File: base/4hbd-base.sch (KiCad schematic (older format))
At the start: 33 parts

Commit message: annotate sch
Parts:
- gave numbers to parts that had none: 33

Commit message: added footprints, created netlist
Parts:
- J8: footprint (none) -> TerminalBlock:SpringTerminalBlock_KF141R_4_P2.54mm
- TP1, TP10, TP11, TP12, TP13, TP14, TP15, TP16, TP17, TP18, TP19, TP2, TP20, TP3, TP4, TP5, TP6, TP7, TP8, TP9: footprint (none) -> TestPoint:TestPoint_Pad_D1.5mm

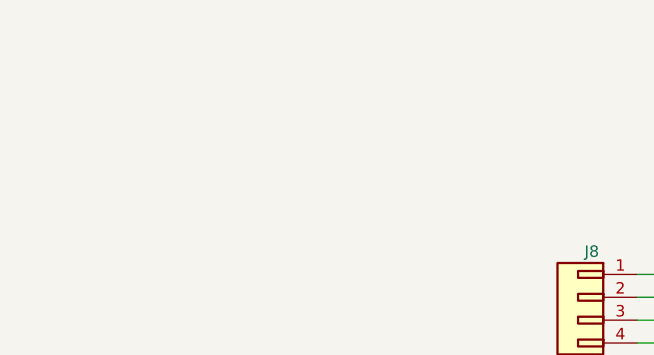
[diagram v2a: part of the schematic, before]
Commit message: mount hole was added
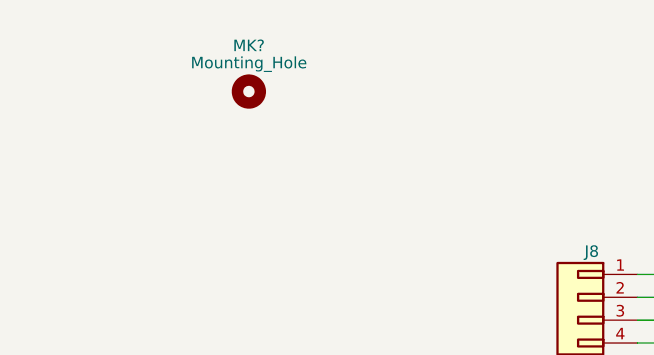
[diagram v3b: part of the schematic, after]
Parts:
- added MK?: Mounting_Hole, symbol Mounting_Hole
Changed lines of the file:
@@
 LIBS:opto
 LIBS:maxim
+LIBS:Mechanical
 LIBS:4hbd-base-cache
 EELAYER 25 0
@@
 	1    0    0    -1
 $EndComp
+$Comp
+L Mounting_Hole MK?
+U 1 1 5A4C234B
+P 900 900
+F 0 "MK?" H 900 1100 50  0000 C CNN
+F 1 "Mounting_Hole" H 900 1025 50  0000 C CNN
+F 2 "" H 900 900 50  0001 C CNN
+F 3 "" H 900 900 50  0001 C CNN
+	1    900  900
+	1    0    0    -1
+$EndComp

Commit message: mount hole
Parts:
- removed J8: Spring_Terminal_Connector_01x04, TerminalBlock:SpringTerminalBlock_KF141R_4_P2.54mm, symbol Spring_Terminal_Connector_01x04
- added J8: Screw_Terminal_01x04, TerminalBlock:TerminalBlock_Altech_AK300-4_P5.00mm, symbol Screw_Terminal_01x04
- added MK2, MK3, MK4: Mounting_Hole, MountingHole:MountingHole_3.5mm_Pad, symbol Mounting_Hole
- MK1: renamed from MK?; footprint (none) -> MountingHole:MountingHole_3.5mm_Pad
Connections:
- net MOSFETs/CurSense/Isolation/HB0s: now also J8.1 (Pin_1)
- net MOSFETs/CurSense/Isolation/HB1: now also J8.2 (Pin_2)
- net MOSFETs/CurSense/Isolation/HB2s: now also J8.3 (Pin_3)
- net MOSFETs/CurSense/Isolation/HB3: now also J8.4 (Pin_4)
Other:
- moved on the sheet: MK1
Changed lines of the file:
@@
 $EndSheet
 $Comp
-L GNDD #PWR01
+L GNDD #PWR12
 U 1 1 5A1C4DF7
 P 8900 6000
-F 0 "#PWR01" H 8900 5750 50  0001 C CNN
+F 0 "#PWR12" H 8900 5750 50  0001 C CNN
 F 1 "GNDD" H 8900 5875 50  0000 C CNN
 F 2 "" H 8900 6000 50  0001 C CNN
@@
 $EndComp
 $Comp
-L GNDD #PWR02
+L GNDD #PWR11
 U 1 1 5A1C5052
 P 8900 3500
-F 0 "#PWR02" H 8900 3250 50  0001 C CNN
+F 0 "#PWR11" H 8900 3250 50  0001 C CNN
 F 1 "GNDD" H 8900 3375 50  0000 C CNN
 F 2 "" H 8900 3500 50  0001 C CNN
@@
 $EndComp
 $Comp
-L GNDD #PWR03
+L GNDD #PWR7
 U 1 1 5A1C5445
 P 4800 5600
-F 0 "#PWR03" H 4800 5350 50  0001 C CNN
+F 0 "#PWR7" H 4800 5350 50  0001 C CNN
 F 1 "GNDD" H 4800 5475 50  0000 C CNN
 F 2 "" H 4800 5600 50  0001 C CNN
@@
 $EndComp
 $Comp
-L GNDD #PWR04
+L GNDD #PWR6
 U 1 1 5A1C7749
 P 4800 3800
-F 0 "#PWR04" H 4800 3550 50  0001 C CNN
+F 0 "#PWR6" H 4800 3550 50  0001 C CNN
 F 1 "GNDD" H 4800 3675 50  0000 C CNN
 F 2 "" H 4800 3800 50  0001 C CNN
@@
 $EndComp
 $Comp
-L GNDD #PWR05
+L GNDD #PWR10
 U 1 1 5A1D2700
 P 8400 4800
-F 0 "#PWR05" H 8400 4550 50  0001 C CNN
+F 0 "#PWR10" H 8400 4550 50  0001 C CNN
 F 1 "GNDD" H 8400 4675 50  0000 C CNN
 F 2 "" H 8400 4800 50  0001 C CNN
@@
 $EndComp
 $Comp
-L GNDD #PWR06
+L GNDD #PWR15
 U 1 1 5A1D7E7F
 P 10650 5500
-F 0 "#PWR06" H 10650 5250 50  0001 C CNN
+F 0 "#PWR15" H 10650 5250 50  0001 C CNN
 F 1 "GNDD" H 10650 5375 50  0000 C CNN
 F 2 "" H 10650 5500 50  0001 C CNN
@@
 $EndSheet
 $Comp
-L GNDD #PWR07
+L GNDD #PWR14
 U 1 1 5A1E3D1F
 P 10600 2500
-F 0 "#PWR07" H 10600 2250 50  0001 C CNN
+F 0 "#PWR14" H 10600 2250 50  0001 C CNN
 F 1 "GNDD" H 10600 2375 50  0000 C CNN
 F 2 "" H 10600 2500 50  0001 C CNN
@@
 $EndComp
 $Comp
-L GNDD #PWR08
+L GNDD #PWR13
 U 1 1 5A1E950D
 P 10200 1750
-F 0 "#PWR08" H 10200 1500 50  0001 C CNN
+F 0 "#PWR13" H 10200 1500 50  0001 C CNN
 F 1 "GNDD" H 10200 1625 50  0000 C CNN
 F 2 "" H 10200 1750 50  0001 C CNN
@@
 $EndComp
 $Comp
-L GNDPWR #PWR09
+L GNDPWR #PWR3
 U 1 1 5A1F43A1
 P 2800 5600
-F 0 "#PWR09" H 2800 5400 50  0001 C CNN
+F 0 "#PWR3" H 2800 5400 50  0001 C CNN
 F 1 "GNDPWR" H 2800 5470 50  0000 C CNN
 F 2 "" H 2800 5550 50  0001 C CNN
@@
 $EndComp
 $Comp
-L GNDPWR #PWR010
+L GNDPWR #PWR1
 U 1 1 5A1F4674
 P 1200 7100
-F 0 "#PWR010" H 1200 6900 50  0001 C CNN
+F 0 "#PWR1" H 1200 6900 50  0001 C CNN
 F 1 "GNDPWR" H 1200 6970 50  0000 C CNN
 F 2 "" H 1200 7050 50  0001 C CNN
@@
 $EndComp
 $Comp
-L GNDPWR #PWR011
+L GNDPWR #PWR2
 U 1 1 5A1F4ECF
 P 2800 3600
-F 0 "#PWR011" H 2800 3400 50  0001 C CNN
+F 0 "#PWR2" H 2800 3400 50  0001 C CNN
 F 1 "GNDPWR" H 2800 3470 50  0000 C CNN
 F 2 "" H 2800 3550 50  0001 C CNN
@@
 $EndSheet
 $Comp
-L GNDD #PWR012
+L GNDD #PWR8
 U 1 1 5A3B40B0
 P 6200 7400
-F 0 "#PWR012" H 6200 7150 50  0001 C CNN
+F 0 "#PWR8" H 6200 7150 50  0001 C CNN
 F 1 "GNDD" H 6200 7275 50  0000 C CNN
 F 2 "" H 6200 7400 50  0001 C CNN
@@
 $EndComp
 $Comp
-L GNDD #PWR013
+L GNDD #PWR5
 U 1 1 5A3B43A6
 P 4600 7000
-F 0 "#PWR013" H 4600 6750 50  0001 C CNN
+F 0 "#PWR5" H 4600 6750 50  0001 C CNN
 F 1 "GNDD" H 4600 6875 50  0000 C CNN
 F 2 "" H 4600 7000 50  0001 C CNN
@@
 Connection ~ 5100 1400
 $Comp
-L GNDD #PWR014
+L GNDD #PWR9
 U 1 1 5A497DD0
 P 7950 6350
-F 0 "#PWR014" H 7950 6100 50  0001 C CNN
+F 0 "#PWR9" H 7950 6100 50  0001 C CNN
 F 1 "GNDD" H 7950 6225 50  0000 C CNN
 F 2 "" H 7950 6350 50  0001 C CNN
@@
 Connection ~ 2850 7400
 $Comp
-L GNDPWR #PWR015
+L GNDPWR #PWR4
 U 1 1 5A49D4A5
 P 3100 7500
-F 0 "#PWR015" H 3100 7300 50  0001 C CNN
+F 0 "#PWR4" H 3100 7300 50  0001 C CNN
 F 1 "GNDPWR" H 3100 7370 50  0000 C CNN
 F 2 "" H 3100 7450 50  0001 C CNN
@@
 $EndComp
 $Comp
-L Spring_Terminal_Connector_01x04 J8
-U 1 1 5A4C5A2B
-P 2400 1800
-F 0 "J8" H 2400 2000 50  0000 C CNN
-F 1 "Spring_Terminal_Connector_01x04" H 2450 1500 50  0000 C CNN
-F 2 "TerminalBlock:SpringTerminalBlock_KF141R_4_P2.54mm" H 2400 1800 50  0001 C CNN
-F 3 "" H 2400 1800 50  0001 C CNN
-	1    2400 1800
-	-1   0    0    -1
-$EndComp
-$Comp
 L Spring_Terminal_Connector_01x08 J12
 U 1 1 5A4CBF24
@@
 $EndComp
 $Comp
-L Mounting_Hole MK?
+L Mounting_Hole MK1
 U 1 1 5A4C234B
-P 900 900
-F 0 "MK?" H 900 1100 50  0000 C CNN
-F 1 "Mounting_Hole" H 900 1025 50  0000 C CNN
-F 2 "" H 900 900 50  0001 C CNN
-F 3 "" H 900 900 50  0001 C CNN
-	1    900  900
-	1    0    0    -1
-$EndComp
+P 850 950
+F 0 "MK1" H 850 1150 50  0000 C CNN
+F 1 "Mounting_Hole" H 850 1075 50  0000 C CNN
+F 2 "MountingHole:MountingHole_3.5mm_Pad" H 850 950 50  0001 C CNN
+F 3 "" H 850 950 50  0001 C CNN
+	1    850  950
+	1    0    0    -1
+$EndComp
+$Comp
+L Screw_Terminal_01x04 J8
+U 1 1 5A4F1133
+P 2400 1800
+F 0 "J8" H 2400 2000 50  0000 C CNN
+F 1 "Screw_Terminal_01x04" H 2400 1500 50  0000 C CNN
+F 2 "TerminalBlock:TerminalBlock_Altech_AK300-4_P5.00mm" H 2400 1800 50  0001 C CNN
+F 3 "" H 2400 1800 50  0001 C CNN
+	1    2400 1800
+	-1   0    0    -1
+$EndComp
+$Comp
+L Mounting_Hole MK2
+U 1 1 5A4F295C
+P 850 1350
+F 0 "MK2" H 850 1550 50  0000 C CNN
+F 1 "Mounting_Hole" H 850 1475 50  0000 C CNN
+F 2 "MountingHole:MountingHole_3.5mm_Pad" H 850 1350 50  0001 C CNN
+F 3 "" H 850 1350 50  0001 C CNN
+	1    850  1350
+	1    0    0    -1
+$EndComp
+$Comp
+L Mounting_Hole MK3
+U 1 1 5A4F2CD9
+P 850 1750
+F 0 "MK3" H 850 1950 50  0000 C CNN
+F 1 "Mounting_Hole" H 850 1875 50  0000 C CNN
+F 2 "MountingHole:MountingHole_3.5mm_Pad" H 850 1750 50  0001 C CNN
+F 3 "" H 850 1750 50  0001 C CNN
+	1    850  1750
+	1    0    0    -1
+$EndComp
+$Comp
+L Mounting_Hole MK4
+U 1 1 5A4F3055
+P 850 2150
+F 0 "MK4" H 850 2350 50  0000 C CNN
+F 1 "Mounting_Hole" H 850 2275 50  0000 C CNN
+F 2 "MountingHole:MountingHole_3.5mm_Pad" H 850 2150 50  0001 C CNN
+F 3 "" H 850 2150 50  0001 C CNN
+	1    850  2150
+	1    0    0    -1
+$EndComp

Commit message: update pcb for TerminalBlock_KaiFeng footprint lib
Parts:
- J1, J10, J11, J2, J3, J4, J9: footprint TerminalBlock:SpringTerminalBlock_KF141R_3_P2.54mm -> TerminalBlock_KaiFeng:TerminalBlock_KaiFeng_KF141R-3_1x03_P2.54mm
- J12: footprint TerminalBlock:SpringTerminalBlock_KF141R_8_P2.54mm -> TerminalBlock_KaiFeng:TerminalBlock_KaiFeng_KF141R-8_1x08_P2.54mm
- J5, J6: footprint TerminalBlock:SpringTerminalBlock_KF141R_2_P2.54mm -> TerminalBlock_KaiFeng:TerminalBlock_KaiFeng_KF141R-2_1x02_P2.54mm
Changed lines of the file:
@@
 F 0 "J1" H 700 3600 50  0000 C CNN
 F 1 "Spring_Terminal_Connector_01x03" H 700 3200 50  0000 C CNN
-F 2 "TerminalBlock:SpringTerminalBlock_KF141R_3_P2.54mm" H 700 3400 50  0001 C CNN
+F 2 "TerminalBlock_KaiFeng:TerminalBlock_KaiFeng_KF141R-3_1x03_P2.54mm" H 700 3400 50  0001 C CNN
 F 3 "" H 700 3400 50  0001 C CNN
 	1    700  3400
@@
 F 0 "J2" H 700 4000 50  0000 C CNN
 F 1 "Spring_Terminal_Connector_01x03" H 700 3600 50  0000 C CNN
-F 2 "TerminalBlock:SpringTerminalBlock_KF141R_3_P2.54mm" H 700 3800 50  0001 C CNN
+F 2 "TerminalBlock_KaiFeng:TerminalBlock_KaiFeng_KF141R-3_1x03_P2.54mm" H 700 3800 50  0001 C CNN
 F 3 "" H 700 3800 50  0001 C CNN
 	1    700  3800
@@
 F 0 "J3" H 700 4400 50  0000 C CNN
 F 1 "Spring_Terminal_Connector_01x03" H 700 4000 50  0000 C CNN
-F 2 "TerminalBlock:SpringTerminalBlock_KF141R_3_P2.54mm" H 700 4200 50  0001 C CNN
+F 2 "TerminalBlock_KaiFeng:TerminalBlock_KaiFeng_KF141R-3_1x03_P2.54mm" H 700 4200 50  0001 C CNN
 F 3 "" H 700 4200 50  0001 C CNN
 	1    700  4200
@@
 F 0 "J4" H 700 4800 50  0000 C CNN
 F 1 "Spring_Terminal_Connector_01x03" H 700 4400 50  0000 C CNN
-F 2 "TerminalBlock:SpringTerminalBlock_KF141R_3_P2.54mm" H 700 4600 50  0001 C CNN
+F 2 "TerminalBlock_KaiFeng:TerminalBlock_KaiFeng_KF141R-3_1x03_P2.54mm" H 700 4600 50  0001 C CNN
 F 3 "" H 700 4600 50  0001 C CNN
 	1    700  4600
@@
 F 0 "J9" H 4300 6500 50  0000 C CNN
 F 1 "Spring_Terminal_Connector_01x03" H 4300 6100 50  0000 C CNN
-F 2 "TerminalBlock:SpringTerminalBlock_KF141R_3_P2.54mm" H 4300 6300 50  0001 C CNN
+F 2 "TerminalBlock_KaiFeng:TerminalBlock_KaiFeng_KF141R-3_1x03_P2.54mm" H 4300 6300 50  0001 C CNN
 F 3 "" H 4300 6300 50  0001 C CNN
 	1    4300 6300
@@
 F 0 "J10" H 4300 6900 50  0000 C CNN
 F 1 "Spring_Terminal_Connector_01x03" H 4300 6500 50  0000 C CNN
-F 2 "TerminalBlock:SpringTerminalBlock_KF141R_3_P2.54mm" H 4300 6700 50  0001 C CNN
+F 2 "TerminalBlock_KaiFeng:TerminalBlock_KaiFeng_KF141R-3_1x03_P2.54mm" H 4300 6700 50  0001 C CNN
 F 3 "" H 4300 6700 50  0001 C CNN
 	1    4300 6700
@@
 F 0 "J11" H 10900 1400 50  0000 C CNN
 F 1 "Spring_Terminal_Connector_01x03" H 10900 1000 50  0000 C CNN
-F 2 "TerminalBlock:SpringTerminalBlock_KF141R_3_P2.54mm" H 10900 1200 50  0001 C CNN
+F 2 "TerminalBlock_KaiFeng:TerminalBlock_KaiFeng_KF141R-3_1x03_P2.54mm" H 10900 1200 50  0001 C CNN
 F 3 "" H 10900 1200 50  0001 C CNN
 	1    10900 1200
@@
 F 0 "J12" H 10900 2700 50  0000 C CNN
 F 1 "Spring_Terminal_Connector_01x08" H 10950 1750 50  0000 C CNN
-F 2 "TerminalBlock:SpringTerminalBlock_KF141R_8_P2.54mm" H 10900 2500 50  0001 C CNN
+F 2 "TerminalBlock_KaiFeng:TerminalBlock_KaiFeng_KF141R-8_1x08_P2.54mm" H 10900 2500 50  0001 C CNN
 F 3 "" H 10900 2500 50  0001 C CNN
 	1    10900 2500
@@
 F 0 "J5" H 700 5200 50  0000 C CNN
 F 1 "Spring_Terminal_Connector_01x02" H 750 4900 50  0000 C CNN
-F 2 "TerminalBlock:SpringTerminalBlock_KF141R_2_P2.54mm" H 700 5000 50  0001 C CNN
+F 2 "TerminalBlock_KaiFeng:TerminalBlock_KaiFeng_KF141R-2_1x02_P2.54mm" H 700 5000 50  0001 C CNN
 F 3 "" H 700 5000 50  0001 C CNN
 	1    700  5000
@@
 F 0 "J6" H 700 5500 50  0000 C CNN
 F 1 "Spring_Terminal_Connector_01x02" H 750 5200 50  0000 C CNN
-F 2 "TerminalBlock:SpringTerminalBlock_KF141R_2_P2.54mm" H 700 5300 50  0001 C CNN
+F 2 "TerminalBlock_KaiFeng:TerminalBlock_KaiFeng_KF141R-2_1x02_P2.54mm" H 700 5300 50  0001 C CNN
 F 3 "" H 700 5300 50  0001 C CNN
 	1    700  5300

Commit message: pcb was edited
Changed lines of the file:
@@
 P 700 3400
 F 0 "J1" H 700 3600 50  0000 C CNN
-F 1 "Spring_Terminal_Connector_01x03" H 700 3200 50  0000 C CNN
+F 1 "Spring_Terminal_Connector_01x03" H 1500 3200 50  0000 C CNN
 F 2 "TerminalBlock_KaiFeng:TerminalBlock_KaiFeng_KF141R-3_1x03_P2.54mm" H 700 3400 50  0001 C CNN
 F 3 "" H 700 3400 50  0001 C CNN
@@
 P 700 3800
 F 0 "J2" H 700 4000 50  0000 C CNN
-F 1 "Spring_Terminal_Connector_01x03" H 700 3600 50  0000 C CNN
+F 1 "Spring_Terminal_Connector_01x03" H 1500 3600 50  0000 C CNN
 F 2 "TerminalBlock_KaiFeng:TerminalBlock_KaiFeng_KF141R-3_1x03_P2.54mm" H 700 3800 50  0001 C CNN
 F 3 "" H 700 3800 50  0001 C CNN
@@
 P 700 4200
 F 0 "J3" H 700 4400 50  0000 C CNN
-F 1 "Spring_Terminal_Connector_01x03" H 700 4000 50  0000 C CNN
+F 1 "Spring_Terminal_Connector_01x03" H 1500 4000 50  0000 C CNN
 F 2 "TerminalBlock_KaiFeng:TerminalBlock_KaiFeng_KF141R-3_1x03_P2.54mm" H 700 4200 50  0001 C CNN
 F 3 "" H 700 4200 50  0001 C CNN
@@
 P 700 4600
 F 0 "J4" H 700 4800 50  0000 C CNN
-F 1 "Spring_Terminal_Connector_01x03" H 700 4400 50  0000 C CNN
+F 1 "Spring_Terminal_Connector_01x03" H 1500 4400 50  0000 C CNN
 F 2 "TerminalBlock_KaiFeng:TerminalBlock_KaiFeng_KF141R-3_1x03_P2.54mm" H 700 4600 50  0001 C CNN
 F 3 "" H 700 4600 50  0001 C CNN
@@
 P 4300 6300
 F 0 "J9" H 4300 6500 50  0000 C CNN
-F 1 "Spring_Terminal_Connector_01x03" H 4300 6100 50  0000 C CNN
+F 1 "Spring_Terminal_Connector_01x03" H 5050 6100 50  0000 C CNN
 F 2 "TerminalBlock_KaiFeng:TerminalBlock_KaiFeng_KF141R-3_1x03_P2.54mm" H 4300 6300 50  0001 C CNN
 F 3 "" H 4300 6300 50  0001 C CNN
@@
 P 4300 6700
 F 0 "J10" H 4300 6900 50  0000 C CNN
-F 1 "Spring_Terminal_Connector_01x03" H 4300 6500 50  0000 C CNN
+F 1 "Spring_Terminal_Connector_01x03" H 4750 6500 50  0000 C CNN
 F 2 "TerminalBlock_KaiFeng:TerminalBlock_KaiFeng_KF141R-3_1x03_P2.54mm" H 4300 6700 50  0001 C CNN
 F 3 "" H 4300 6700 50  0001 C CNN
@@
 P 700 5000
 F 0 "J5" H 700 5200 50  0000 C CNN
-F 1 "Spring_Terminal_Connector_01x02" H 750 4900 50  0000 C CNN
+F 1 "Spring_Terminal_Connector_01x02" H 1500 4900 50  0000 C CNN
 F 2 "TerminalBlock_KaiFeng:TerminalBlock_KaiFeng_KF141R-2_1x02_P2.54mm" H 700 5000 50  0001 C CNN
 F 3 "" H 700 5000 50  0001 C CNN
@@
 P 700 5300
 F 0 "J6" H 700 5500 50  0000 C CNN
-F 1 "Spring_Terminal_Connector_01x02" H 750 5200 50  0000 C CNN
+F 1 "Spring_Terminal_Connector_01x02" H 1500 5200 50  0000 C CNN
 F 2 "TerminalBlock_KaiFeng:TerminalBlock_KaiFeng_KF141R-2_1x02_P2.54mm" H 700 5300 50  0001 C CNN
 F 3 "" H 700 5300 50  0001 C CNN

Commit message: current pcb
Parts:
- MK1, MK2, MK3, MK4: footprint MountingHole:MountingHole_3.5mm_Pad -> MountingHole:MountingHole_3.5mm
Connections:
- net Digital DC/DC/+24VD: now also J13.2 (Pin_2); no longer J13.1 (Pin_1)
- net GNDD: now also J13.1 (Pin_1); no longer J13.2 (Pin_2)
- net GNDPWR: now also J7.1 (Pin_1); no longer J7.3 (Pin_3)
- net MOSFETs/CurSense/Isolation/Vpwr: now also J7.2 (Pin_2); no longer J7.1 (Pin_1)
- net Power DC/DC/+24VP: now also J7.3 (Pin_3); no longer J7.2 (Pin_2)
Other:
- moved on the sheet: J13
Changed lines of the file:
@@
 L GNDD #PWR06
 U 1 1 5A1D7E7F
-P 10650 5500
-F 0 "#PWR06" H 10650 5250 50  0001 C CNN
-F 1 "GNDD" H 10650 5375 50  0000 C CNN
-F 2 "" H 10650 5500 50  0001 C CNN
-F 3 "" H 10650 5500 50  0001 C CNN
-	1    10650 5500
+P 10700 5150
+F 0 "#PWR06" H 10700 4900 50  0001 C CNN
+F 1 "GNDD" H 10700 5025 50  0000 C CNN
+F 2 "" H 10700 5150 50  0001 C CNN
+F 3 "" H 10700 5150 50  0001 C CNN
+	1    10700 5150
 	0    1    1    0
 $EndComp
@@
 	9100 2900 8200 2900
 Wire Wire Line
-	10300 5400 10750 5400
-Wire Wire Line
-	10750 5500 10650 5500
-Wire Wire Line
 	4600 3300 6900 3300
 Wire Wire Line
@@
 	2800 5500 2800 5600
 Wire Wire Line
-	1200 7000 1400 7000
+	950  7000 1400 7000
 Wire Wire Line
 	2600 6800 2300 6800
@@
 	2500 3300 3000 3300
 Wire Wire Line
-	1300 6800 900  6800
-Wire Wire Line
-	900  6700 1400 6700
-Wire Wire Line
-	900  6600 1100 6600
-Wire Wire Line
-	1100 6600 1100 3200
+	1100 3200 1100 6500
 Wire Wire Line
 	1100 3200 3000 3200
@@
 	2600 2000 3000 2000
 Wire Wire Line
-	1200 7000 1200 7100
-Wire Wire Line
-	1300 3500 1300 7000
+	1300 3500 1300 7100
 Connection ~ 1300 7000
-Connection ~ 1300 6800
 Wire Wire Line
 	1200 3300 1200 6700
@@
 L Screw_Terminal_01x02 J13
 U 1 1 5A4C5EB8
-P 10950 5400
-F 0 "J13" H 10950 5500 50  0000 C CNN
-F 1 "Screw_Terminal_01x02" H 10950 5200 50  0000 C CNN
-F 2 "TerminalBlock:TerminalBlock_Altech_AK300-2_P5.00mm" H 10950 5400 50  0001 C CNN
-F 3 "" H 10950 5400 50  0001 C CNN
-	1    10950 5400
+P 10950 5300
+F 0 "J13" H 10950 5400 50  0000 C CNN
+F 1 "Screw_Terminal_01x02" H 10950 5100 50  0000 C CNN
+F 2 "TerminalBlock:TerminalBlock_Altech_AK300-2_P5.00mm" H 10950 5300 50  0001 C CNN
+F 3 "" H 10950 5300 50  0001 C CNN
+	1    10950 5300
 	1    0    0    -1
 $EndComp
@@
 F 0 "MK1" H 850 1150 50  0000 C CNN
 F 1 "Mounting_Hole" H 850 1075 50  0000 C CNN
-F 2 "MountingHole:MountingHole_3.5mm_Pad" H 850 950 50  0001 C CNN
+F 2 "MountingHole:MountingHole_3.5mm" H 850 950 50  0001 C CNN
 F 3 "" H 850 950 50  0001 C CNN
 	1    850  950
@@
 F 0 "MK2" H 850 1550 50  0000 C CNN
 F 1 "Mounting_Hole" H 850 1475 50  0000 C CNN
-F 2 "MountingHole:MountingHole_3.5mm_Pad" H 850 1350 50  0001 C CNN
+F 2 "MountingHole:MountingHole_3.5mm" H 850 1350 50  0001 C CNN
 F 3 "" H 850 1350 50  0001 C CNN
 	1    850  1350
@@
 F 0 "MK3" H 850 1950 50  0000 C CNN
 F 1 "Mounting_Hole" H 850 1875 50  0000 C CNN
-F 2 "MountingHole:MountingHole_3.5mm_Pad" H 850 1750 50  0001 C CNN
+F 2 "MountingHole:MountingHole_3.5mm" H 850 1750 50  0001 C CNN
 F 3 "" H 850 1750 50  0001 C CNN
 	1    850  1750
@@
 F 0 "MK4" H 850 2350 50  0000 C CNN
 F 1 "Mounting_Hole" H 850 2275 50  0000 C CNN
-F 2 "MountingHole:MountingHole_3.5mm_Pad" H 850 2150 50  0001 C CNN
+F 2 "MountingHole:MountingHole_3.5mm" H 850 2150 50  0001 C CNN
 F 3 "" H 850 2150 50  0001 C CNN
 	1    850  2150
 	1    0    0    -1
 $EndComp
+Wire Wire Line
+	1100 6700 1400 6700
+Connection ~ 1200 6600
+Wire Wire Line
+	900  6800 1100 6800
+Wire Wire Line
+	1100 6800 1100 6700
+Wire Wire Line
+	900  6600 950  6600
+Wire Wire Line
+	950  6600 950  7000
+Wire Wire Line
+	1300 7100 1200 7100
+Wire Wire Line
+	900  6700 1050 6700
+Wire Wire Line
+	1050 6700 1050 6500
+Wire Wire Line
+	1050 6500 1100 6500
+Wire Wire Line
+	10300 5400 10750 5400
+Wire Wire Line
+	10750 5300 10750 5150
+Wire Wire Line
+	10750 5150 10700 5150
 $EndSCHEMATC
